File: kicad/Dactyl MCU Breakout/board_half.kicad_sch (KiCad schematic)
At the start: 34 parts, among them J202 Split, J203 Column, J204 Thumb, J205 External, J206 Row, J207 Display, J208 Vic, J301 JST, SW201 Battery, SW202 Reset, SW203 LED, U201 SRV05-4, U202 Nice!Nano/2040

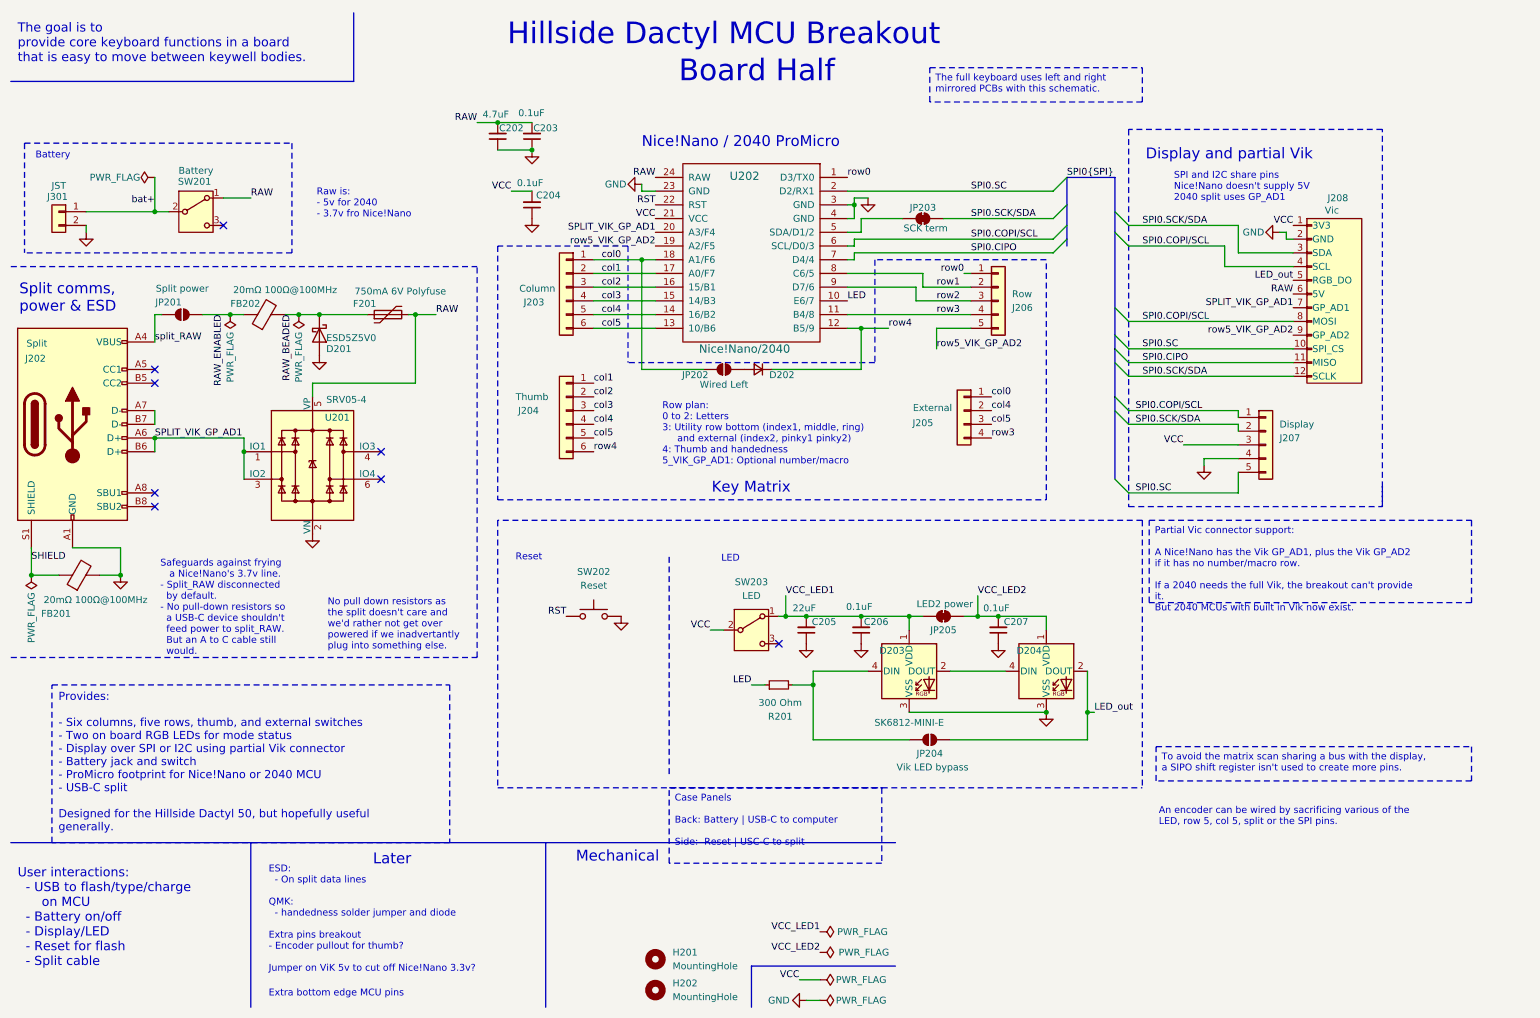
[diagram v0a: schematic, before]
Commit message: feat(pcb): route all but a few traces
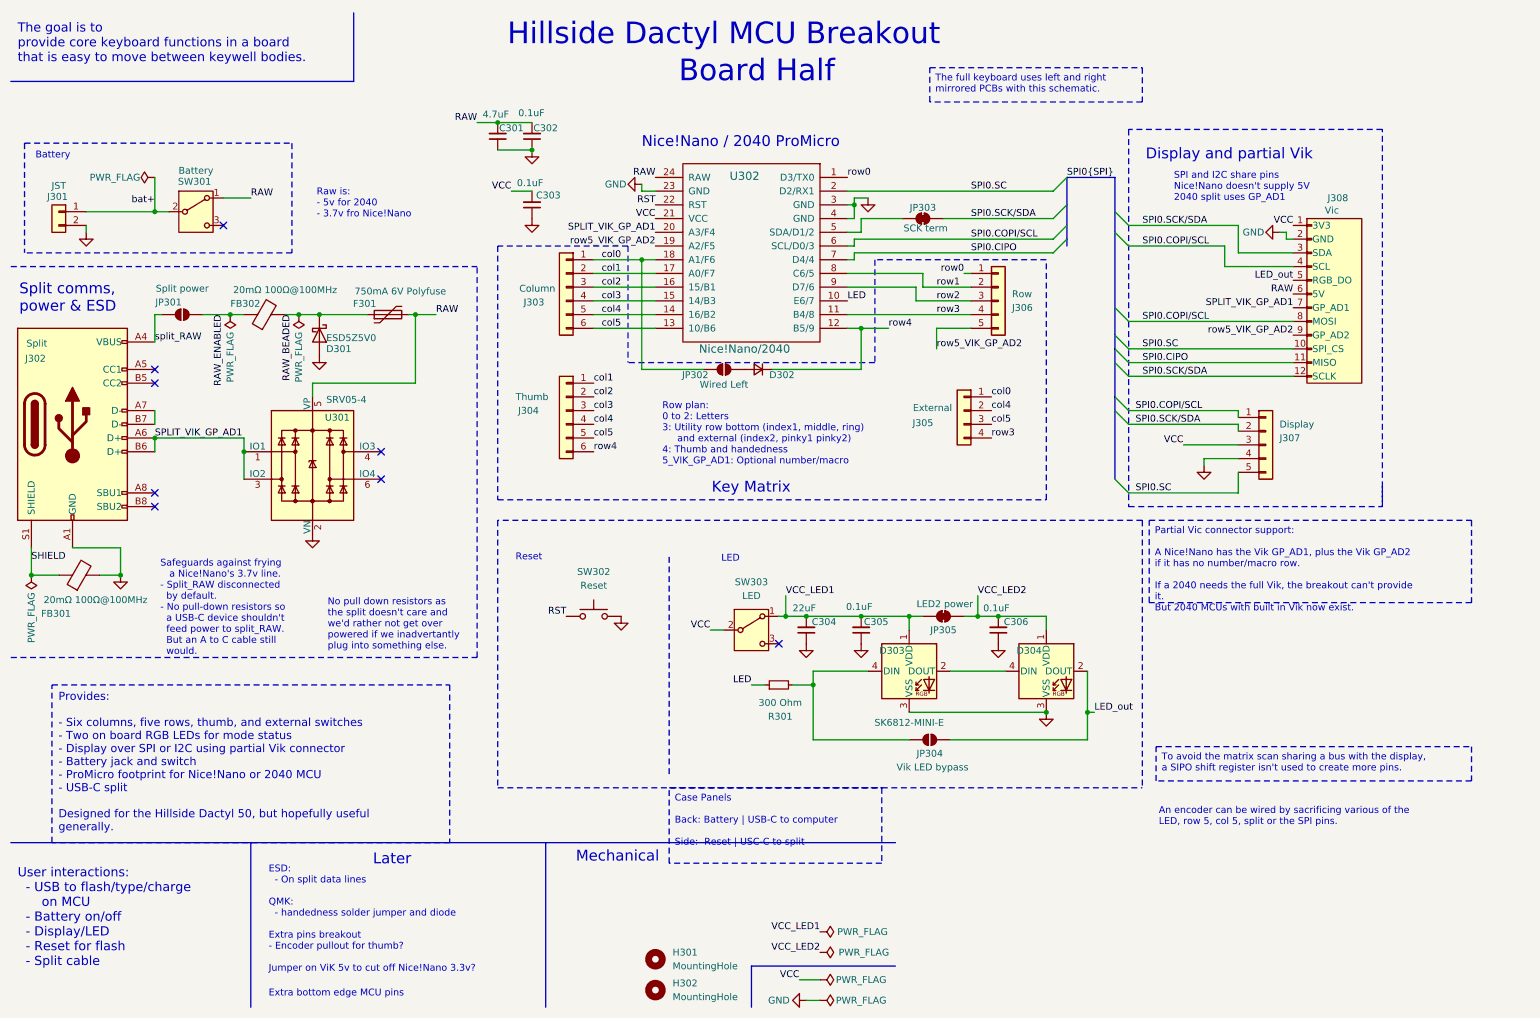
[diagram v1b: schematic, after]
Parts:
- renumbered C202 to C301, C203 to C302, C204 to C303, C205 to C304, C206 to C305, C207 to C306, D201 to D301, D202 to D302, D203 to D303, D204 to D304, F201 to F301, FB201 to FB301, FB202 to FB302, H201 to H301, H202 to H302, J202 to J302, J203 to J303, J204 to J304, J205 to J305, J206 to J306, J207 to J307, J208 to J308, JP201 to JP301, JP202 to JP302, JP203 to JP303, JP204 to JP304, JP205 to JP305, R201 to R301, SW201 to SW301, SW202 to SW302, SW203 to SW303, U201 to U301, U202 to U302

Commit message: feat: make GND local to board half
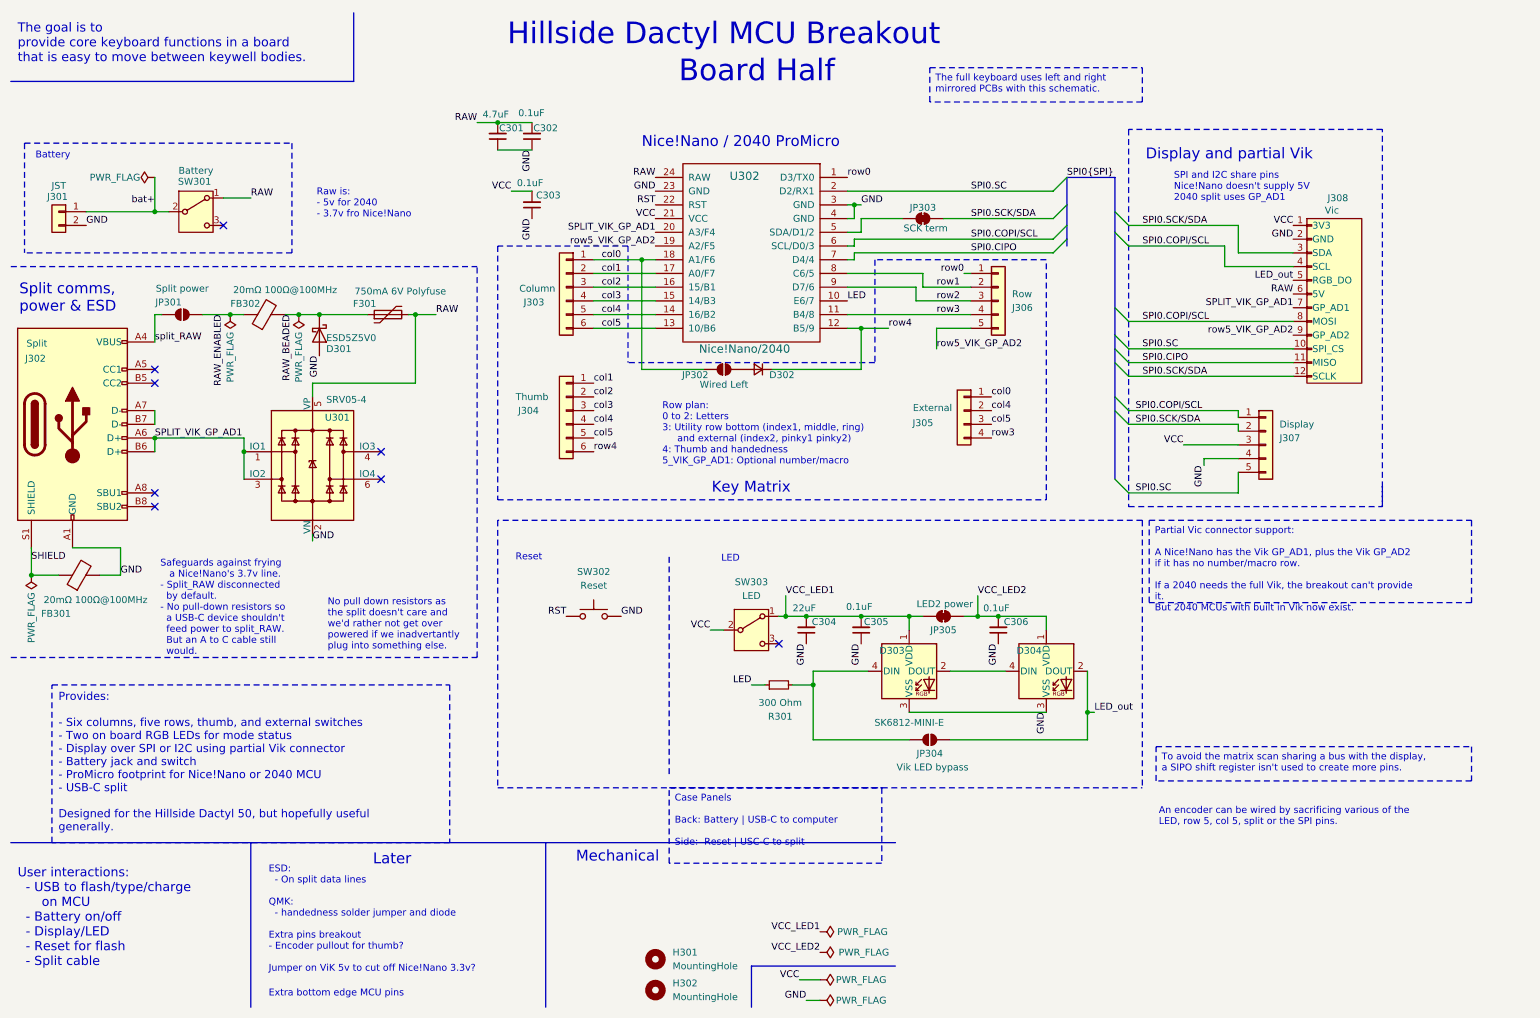
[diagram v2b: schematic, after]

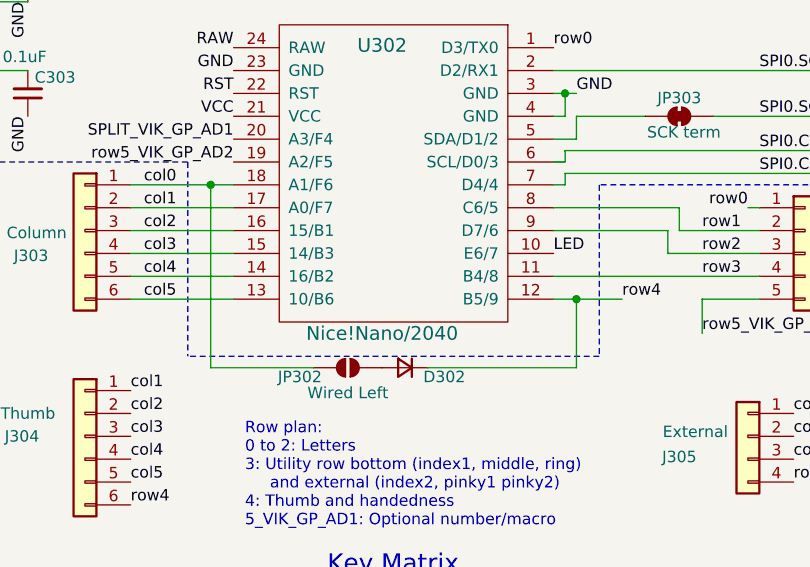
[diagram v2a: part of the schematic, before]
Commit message: feat: handedness jumper only on left board
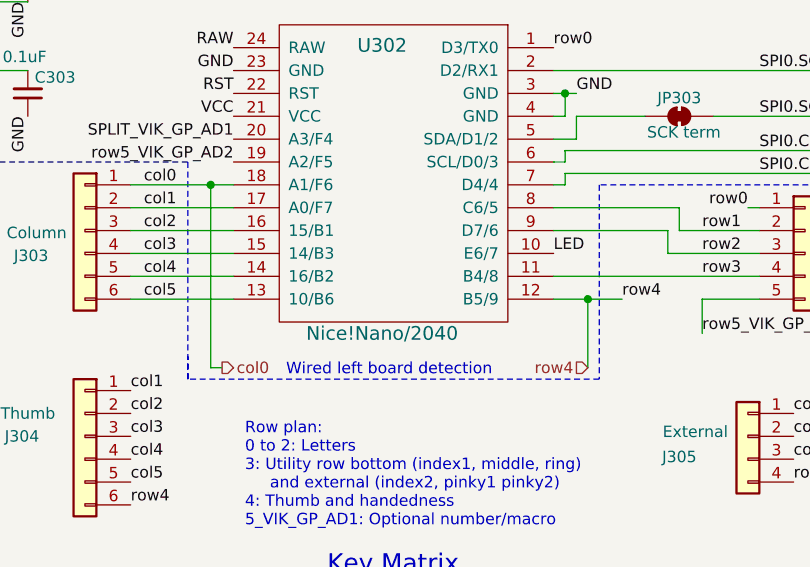
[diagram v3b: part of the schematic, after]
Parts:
- removed D302: D_Small, Diode_SMD:D_SOD-323, symbol Device:D_Small
- removed JP302: Wired Left, Dactyl_basics:SolderJumper-2_P1.3mm_Open_RoundedPad1.0x1.5mm, symbol Jumper:SolderJumper_2_Open
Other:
- note added: "Wired left board detection"

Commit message: feat(schema): clean up part data
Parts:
- F301: LCSC Part C116173 -> C116173
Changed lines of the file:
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@@
 			)
 		)
-		(property "LCSC Part" " C116173"
+		(property "LCSC Part" "C116173"
 			(at 82.55 68.58 0)
 			(effects

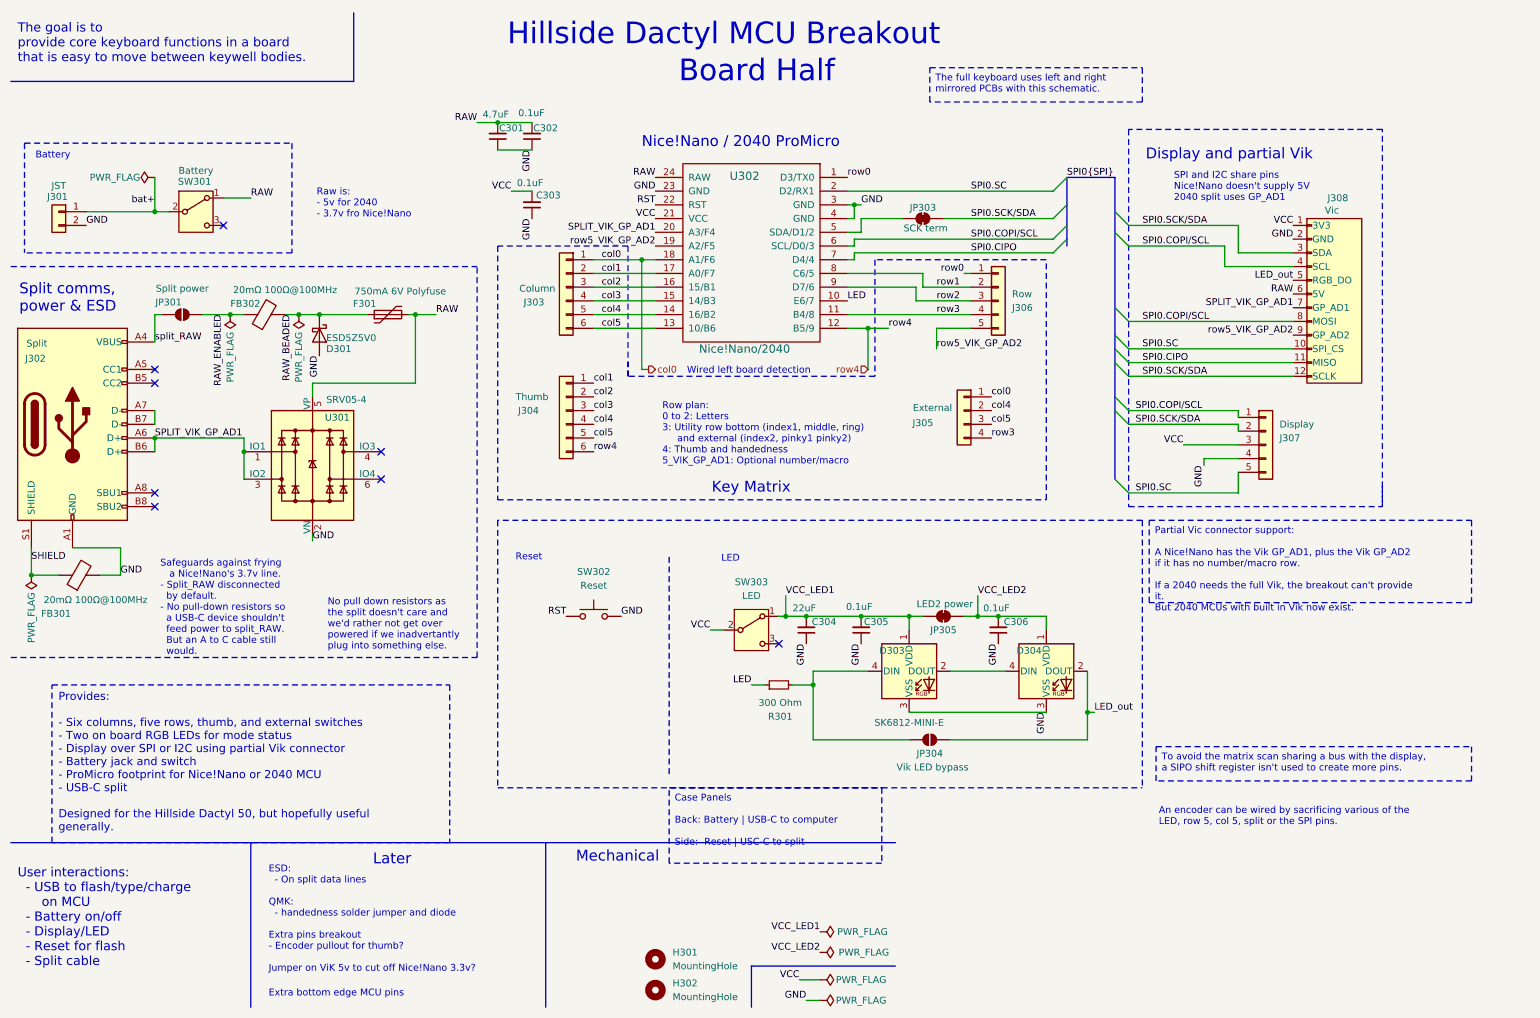
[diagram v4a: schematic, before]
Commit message: feat: larger close capacitors, top/bottom fill
- Solder jumpers for split or battery to reduce the risk of attaching both.
- Wider 0.5 mm tracks for power.
- LED isolation capacitors have smaller loop distance and higher uF within size.
- USB shield ground routed to mount hole pad, as no better place to go.
- Ground fill for top and bottom layers, as well as the middle layer ones.
- Artwork in copper of a small house on a wooded hillside next to a stream.
- Rail copper fills without isolated fill warnings.
- Test point for split data line.
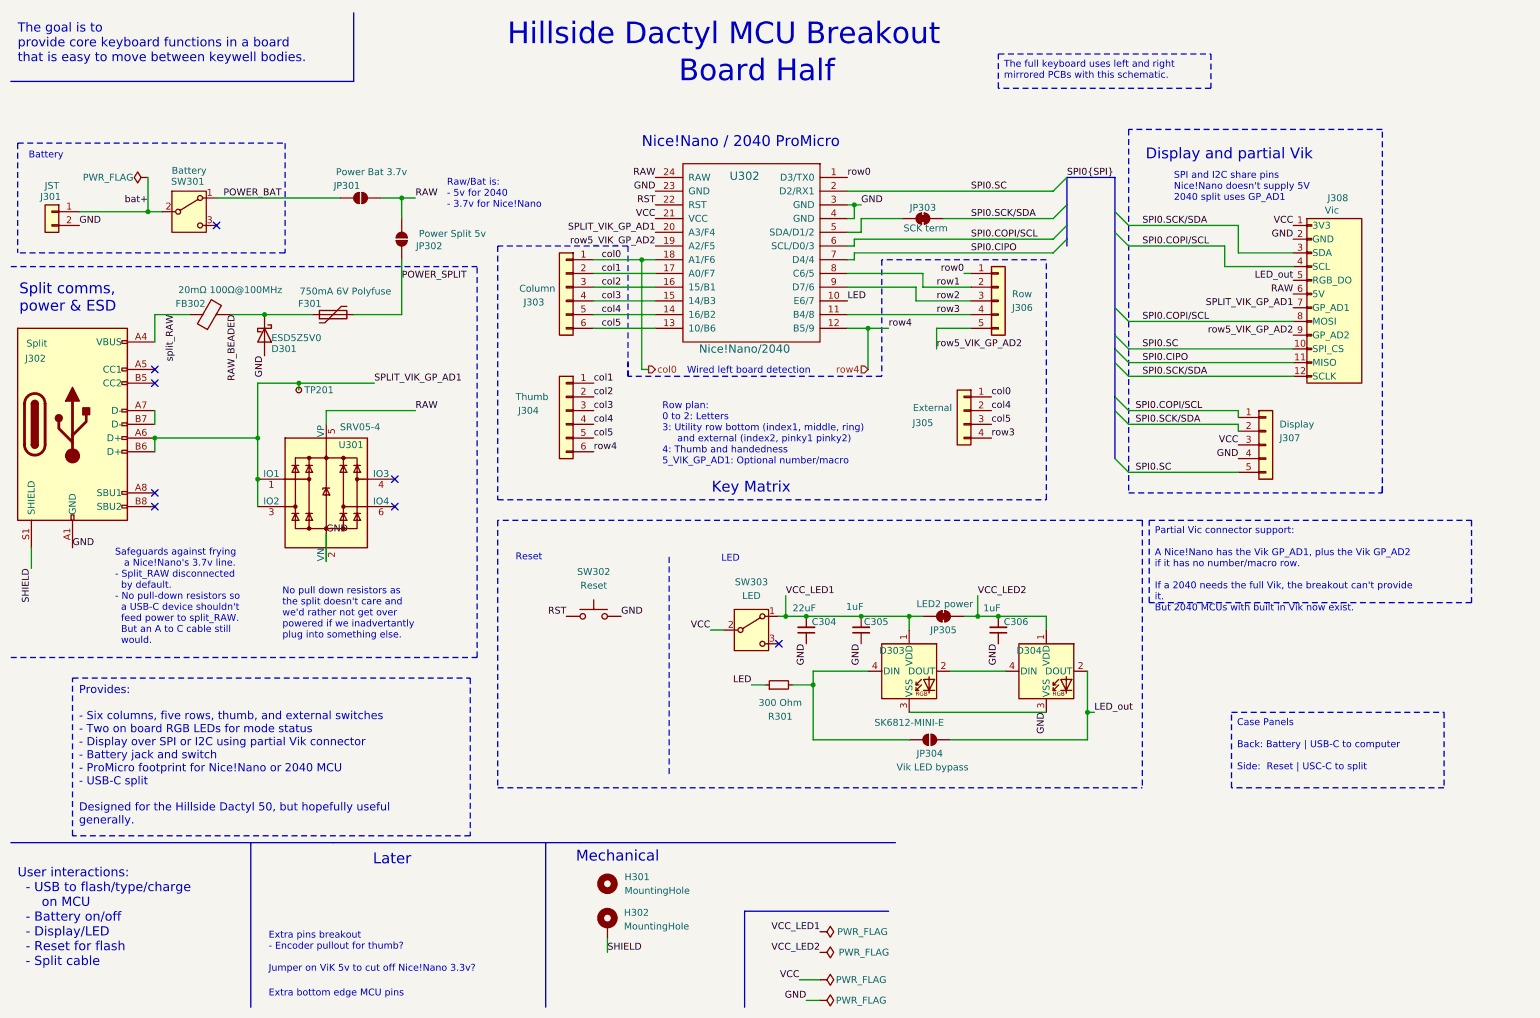
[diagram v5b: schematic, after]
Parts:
- removed C301: 4.7uF, Capacitor_SMD:C_0805_2012Metric, symbol Device:C_Small
- removed C302, C303: 0.1uF, Capacitor_SMD:C_0402_1005Metric, symbol Device:C_Small
- removed FB301: 20mΩ 100Ω@100MHz, Inductor_SMD:L_0805_2012Metric, symbol Device:FerriteBead
- added JP302: Power Split 5v, Dactyl_basics:SolderJumper-2_P1.3mm_Open_RoundedPad1.0x1.5mm, symbol Jumper:SolderJumper_2_Open
- added TP201: TestPoint_Small, TestPoint:TestPoint_THTPad_D1.0mm_Drill0.5mm, symbol Connector:TestPoint_Small
- C304: Role ESD basic -> Power delivery
- C305, C306: value 0.1uF -> 1uF; LCSC Part C1525 -> C52923; Role ESD basic -> Power delivery
- H302: footprint Dactyl_basics:MountingHole_3.2mm_M3_DIN965 -> MountingHole:MountingHole_3.2mm_M3_DIN965_Pad; symbol Mechanical:MountingHole -> Mechanical:MountingHole_Pad
- JP301: value Split power -> Power Bat 3.7v
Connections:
- net RAW: now also JP301.2 (B), JP302.2 (B); no longer F301.2, SW301.1 (A)
- net SHIELD: now also H302.1
- net SPLIT_VIK_GP_AD1: now also TP201.1
- net split_RAW: now also FB302.1; no longer JP301.1 (A)
- removed net RAW_ENABLED: FB302.1, JP301.2 (B)
- new net POWER_BAT: JP301.1 (A), SW301.1 (A)
- new net POWER_SPLIT: F301.2, JP302.1 (A)
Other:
- note added: "Extra pins breakout - Encoder pullout for thumb? Jumper on ViK 5v to cut off Nice!Nano 3.3v?"
- note added: "Raw/Bat is: - 5v for 2040 - 3.7v for Nice!Nano"
- note removed: "An encoder can be wired by sacrificing various of the LED, row 5, col 5, split or the SPI pins."
- note removed: "ESD: - On split data lines QMK: - handedness solder jumper and diode Extra pins breakout - Encoder pullout for thumb? Jumper on ViK 5v to cut off Nice!Nano 3.3v?"
- note removed: "Raw is: - 5v for 2040 - 3.7v fro Nice!Nano"
- moved on the sheet: D301, F301, FB302, H301, J301, SW301, U301

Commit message: feat: cleanup art layout
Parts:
- renumbered TP201 to TP301
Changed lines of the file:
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@@
 	(wire
 		(pts
-			(xy 158.75 191.77) (xy 162.56 191.77)
+			(xy 160.02 191.77) (xy 162.56 191.77)
 		)
 		(stroke
@@
 	(text "Raw/Bat is:\n- 5v for 2040\n- 3.7v for Nice!Nano"
 		(exclude_from_sim no)
-		(at 93.472 49.022 0)
+		(at 92.964 48.514 0)
 		(effects
 			(font
@@
 	)
 	(label "VCC"
-		(at 158.75 191.77 180)
+		(at 160.02 191.77 180)
 		(fields_autoplaced yes)
 		(effects
@@
 	)
 	(label "SHIELD"
-		(at 16.51 115.57 270)
+		(at 16.51 115.57 0)
 		(fields_autoplaced yes)
 		(effects
@@
 				(size 1.27 1.27)
 			)
-			(justify right bottom)
+			(justify left bottom)
 		)
 	)
@@
 		(on_board yes)
 		(dnp no)
-		(property "Reference" "TP201"
+		(property "Reference" "TP301"
 			(at 67.056 82.55 0)
 			(effects
